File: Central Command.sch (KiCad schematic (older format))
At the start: 18 parts

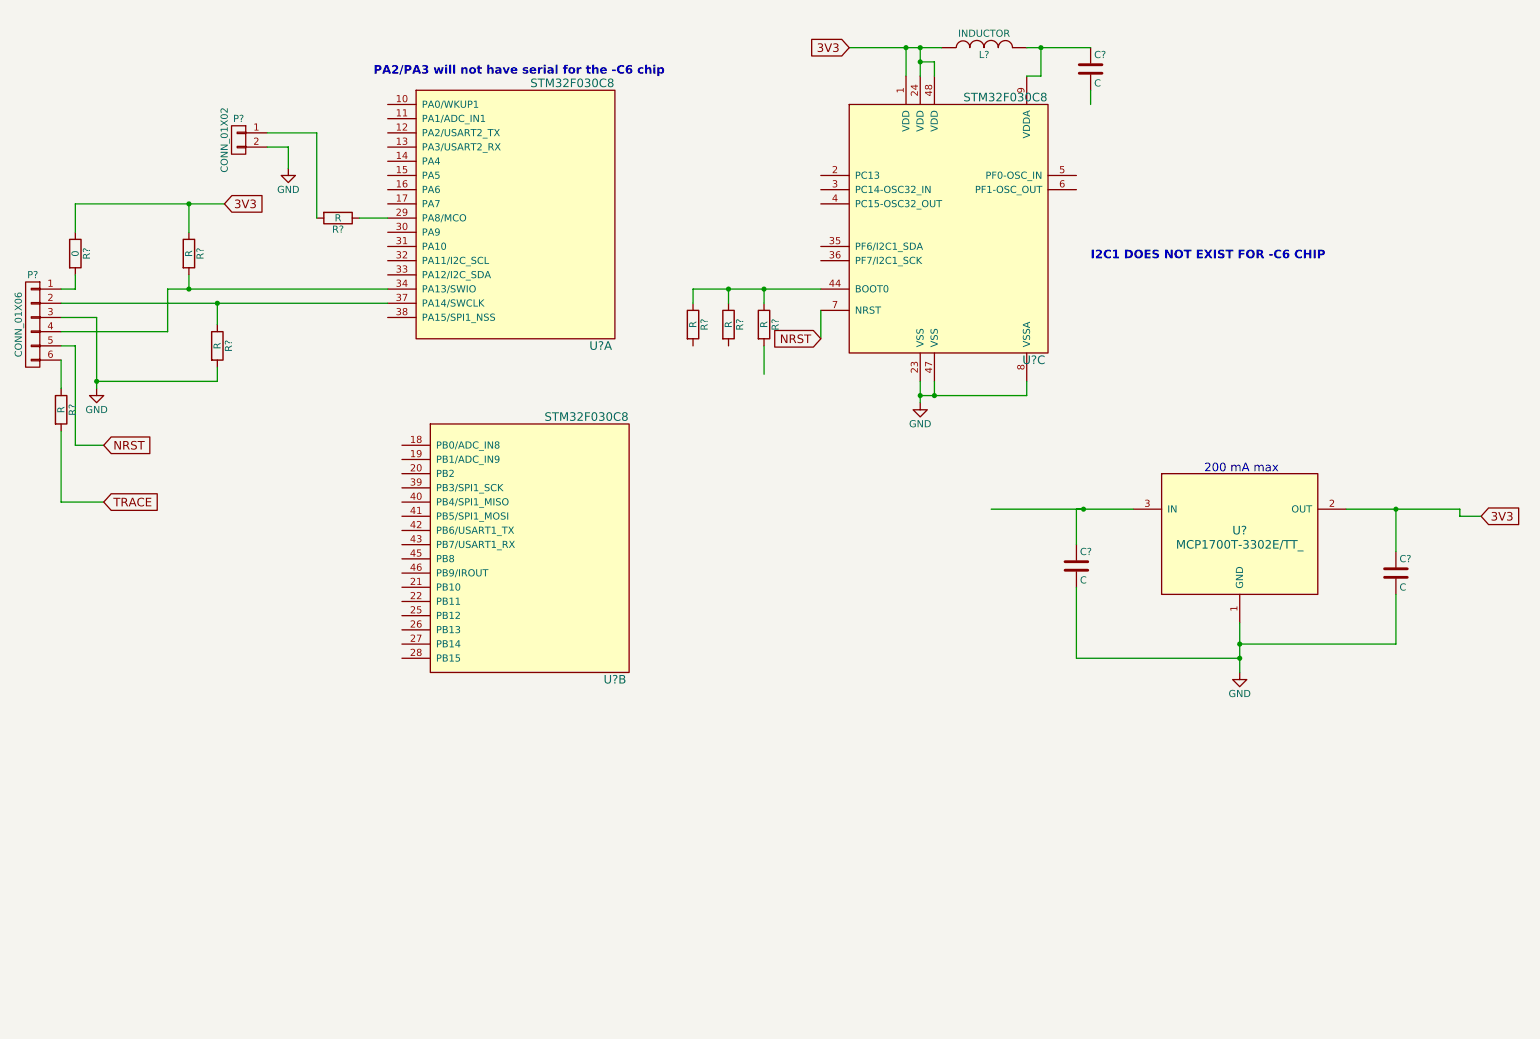
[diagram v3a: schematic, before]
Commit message: Created layout, imported main 48 pin QFP
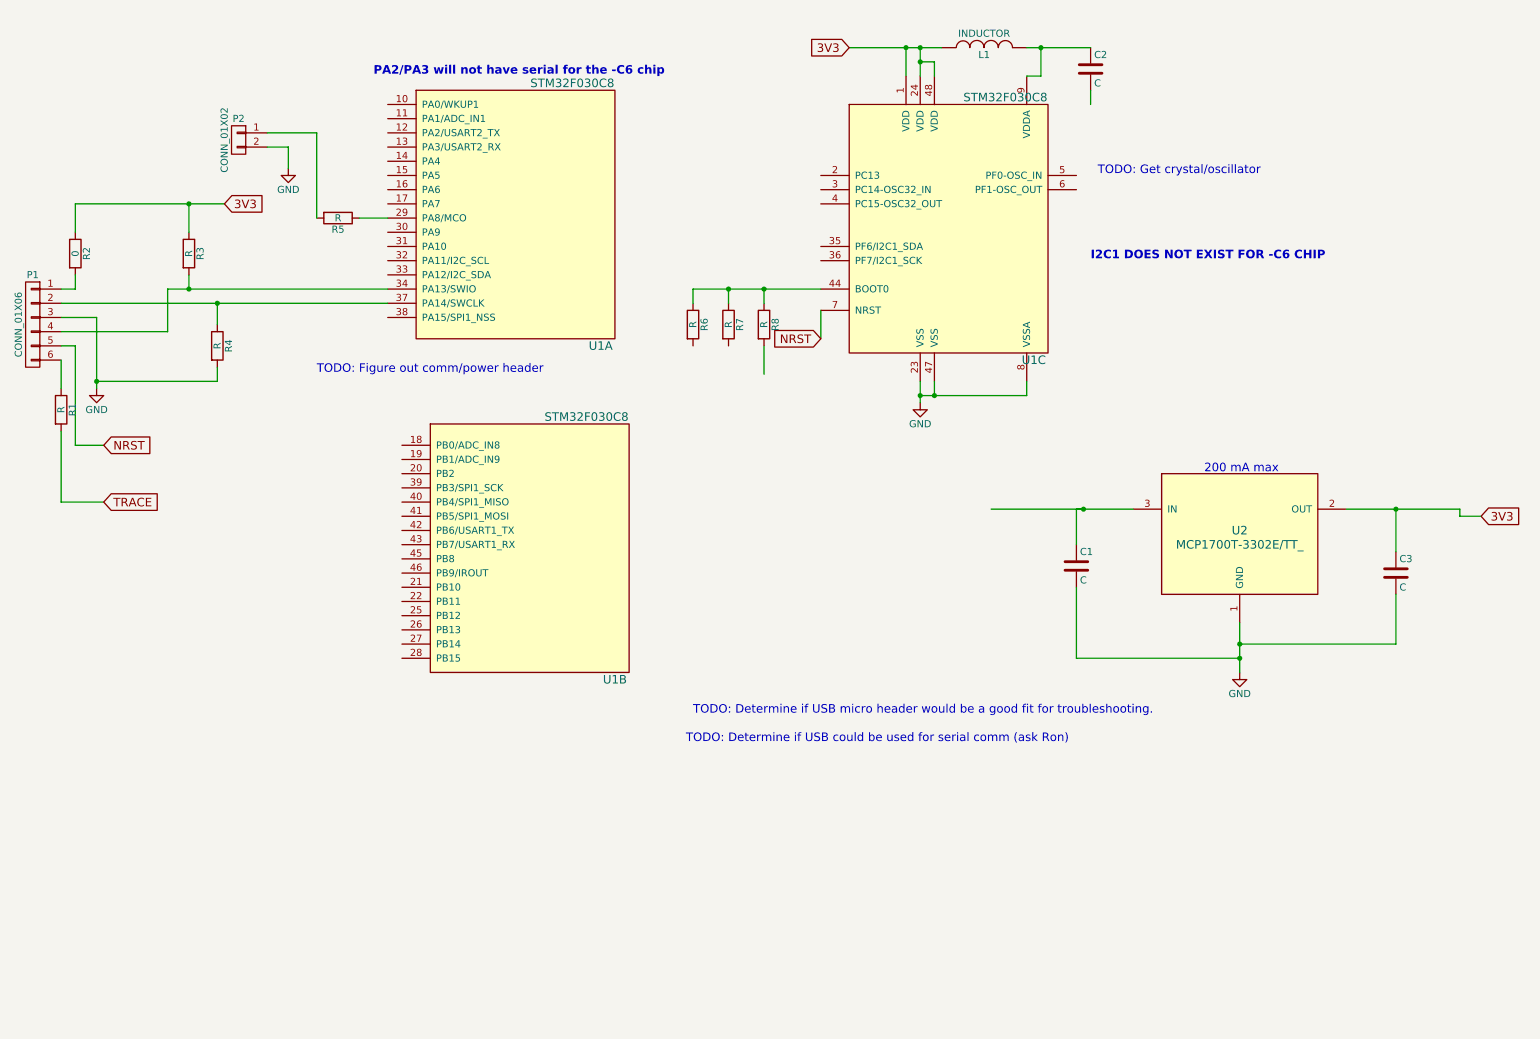
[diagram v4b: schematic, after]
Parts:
- C1, C2, C3: renamed from C?; footprint (none) -> Capacitors_SMD:C_0805
- L1: renamed from L?; footprint (none) -> Inductors_NEOSID:Neosid_Inductor_SM1206
- P1: renamed from P?; footprint (none) -> Pin_Headers:Pin_Header_Straight_1x06
- P2: renamed from P?; footprint (none) -> Pin_Headers:Pin_Header_Straight_1x02
- R1, R2, R3, R4, R5, R6, R7, R8: renamed from R?; footprint (none) -> Resistors_SMD:R_0805
- U1: renamed from U?; footprint (none) -> Housings_QFP:LQFP-48_7x7mm_Pitch0.5mm
- U2: renamed from U?; footprint (none) -> Housings_SOT-23_SOT-143_TSOT-6:SOT-23
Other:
- note added: "TODO: Determine if USB could be used for serial comm (ask Ron)"
- note added: "TODO: Determine if USB micro header would be a good fit for troubleshooting."
- note added: "TODO: Figure out comm/power header"
- note added: "TODO: Get crystal/oscillator"
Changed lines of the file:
@@
 $EndDescr
 $Comp
-L INDUCTOR L?
+L INDUCTOR L1
 U 1 1 5626F24B
 P 7250 800
-F 0 "L?" V 7200 800 50  0000 C CNN
+F 0 "L1" V 7200 800 50  0000 C CNN
 F 1 "INDUCTOR" V 7350 800 50  0000 C CNN
-F 2 "" H 7250 800 60  0000 C CNN
+F 2 "Inductors_NEOSID:Neosid_Inductor_SM1206" H 7250 800 60  0001 C CNN
 F 3 "" H 7250 800 60  0000 C CNN
 	1    7250 800
@@
 $EndComp
 $Comp
-L C C?
+L C C2
 U 1 1 5626F380
 P 8000 950
-F 0 "C?" H 8025 1050 50  0000 L CNN
+F 0 "C2" H 8025 1050 50  0000 L CNN
 F 1 "C" H 8025 850 50  0000 L CNN
-F 2 "" H 8038 800 30  0000 C CNN
+F 2 "Capacitors_SMD:C_0805" H 8038 800 30  0001 C CNN
 F 3 "" H 8000 950 60  0000 C CNN
 	1    8000 950
@@
 $EndComp
 $Comp
-L MCP1700T-3302E/TT_ U?
+L MCP1700T-3302E/TT_ U2
 U 1 1 56270053
 P 9050 4200
-F 0 "U?" H 9050 4200 60  0000 C CNN
+F 0 "U2" H 9050 4200 60  0000 C CNN
 F 1 "MCP1700T-3302E/TT_" H 9050 4100 60  0000 C CNN
-F 2 "" H 9050 4200 60  0000 C CNN
+F 2 "Housings_SOT-23_SOT-143_TSOT-6:SOT-23" H 9050 4200 60  0001 C CNN
 F 3 "" H 9050 4200 60  0000 C CNN
 F 4 "http://parts.io/detail/1370896/MCP1700T-3302E%2FTT" H 9050 4200 60  0001 C CNN "Link"
@@
 $EndComp
 $Comp
-L C C?
+L C C1
 U 1 1 5627009A
 P 7900 4450
-F 0 "C?" H 7925 4550 50  0000 L CNN
+F 0 "C1" H 7925 4550 50  0000 L CNN
 F 1 "C" H 7925 4350 50  0000 L CNN
-F 2 "" H 7938 4300 30  0000 C CNN
+F 2 "Capacitors_SMD:C_0805" H 7938 4300 30  0001 C CNN
 F 3 "" H 7900 4450 60  0000 C CNN
 	1    7900 4450
@@
 $EndComp
 $Comp
-L C C?
+L C C3
 U 1 1 56270119
 P 10150 4500
-F 0 "C?" H 10175 4600 50  0000 L CNN
+F 0 "C3" H 10175 4600 50  0000 L CNN
 F 1 "C" H 10175 4400 50  0000 L CNN
-F 2 "" H 10188 4350 30  0000 C CNN
+F 2 "Capacitors_SMD:C_0805" H 10188 4350 30  0001 C CNN
 F 3 "" H 10150 4500 60  0000 C CNN
 	1    10150 4500
@@
 $EndComp
 $Comp
-L GND #PWR?
+L GND #PWR01
 U 1 1 562701EB
 P 9050 5200
-F 0 "#PWR?" H 9050 4950 50  0001 C CNN
+F 0 "#PWR01" H 9050 4950 50  0001 C CNN
 F 1 "GND" H 9050 5050 50  0000 C CNN
 F 2 "" H 9050 5200 60  0000 C CNN
@@
 3V3
 $Comp
-L GND #PWR?
+L GND #PWR02
 U 1 1 5627066D
 P 6800 3300
-F 0 "#PWR?" H 6800 3050 50  0001 C CNN
+F 0 "#PWR02" H 6800 3050 50  0001 C CNN
 F 1 "GND" H 6800 3150 50  0000 C CNN
 F 2 "" H 6800 3300 60  0000 C CNN
@@
 200 mA max
 $Comp
-L R R?
+L R R8
 U 1 1 562D2D9E
 P 5700 2750
-F 0 "R?" V 5780 2750 50  0000 C CNN
+F 0 "R8" V 5780 2750 50  0000 C CNN
 F 1 "R" V 5700 2750 50  0000 C CNN
-F 2 "" V 5630 2750 30  0000 C CNN
+F 2 "Resistors_SMD:R_0805" V 5630 2750 30  0001 C CNN
 F 3 "" H 5700 2750 30  0000 C CNN
 	1    5700 2750
@@
 $EndComp
 $Comp
-L R R?
+L R R7
 U 1 1 562D2E53
 P 5450 2750
-F 0 "R?" V 5530 2750 50  0000 C CNN
+F 0 "R7" V 5530 2750 50  0000 C CNN
 F 1 "R" V 5450 2750 50  0000 C CNN
-F 2 "" V 5380 2750 30  0000 C CNN
+F 2 "Resistors_SMD:R_0805" V 5380 2750 30  0001 C CNN
 F 3 "" H 5450 2750 30  0000 C CNN
 	1    5450 2750
@@
 $EndComp
 $Comp
-L R R?
+L R R6
 U 1 1 562D2EC7
 P 5200 2750
-F 0 "R?" V 5280 2750 50  0000 C CNN
+F 0 "R6" V 5280 2750 50  0000 C CNN
 F 1 "R" V 5200 2750 50  0000 C CNN
-F 2 "" V 5130 2750 30  0000 C CNN
+F 2 "Resistors_SMD:R_0805" V 5130 2750 30  0001 C CNN
 F 3 "" H 5200 2750 30  0000 C CNN
 	1    5200 2750
@@
 $EndComp
 $Comp
-L CONN_01X06 P?
+L CONN_01X06 P1
 U 1 1 562D3447
 P 550 2750
-F 0 "P?" H 550 3100 50  0000 C CNN
+F 0 "P1" H 550 3100 50  0000 C CNN
 F 1 "CONN_01X06" V 650 2750 50  0000 C CNN
-F 2 "" H 550 2750 60  0000 C CNN
+F 2 "Pin_Headers:Pin_Header_Straight_1x06" H 550 2750 60  0001 C CNN
 F 3 "" H 550 2750 60  0000 C CNN
 	1    550  2750
@@
 	850  1900 850  2100
 $Comp
-L R R?
+L R R2
 U 1 1 562D36B1
 P 850 2250
-F 0 "R?" V 930 2250 50  0000 C CNN
+F 0 "R2" V 930 2250 50  0000 C CNN
 F 1 "0" V 850 2250 50  0000 C CNN
-F 2 "" V 780 2250 30  0000 C CNN
+F 2 "Resistors_SMD:R_0805" V 780 2250 30  0001 C CNN
 F 3 "" H 850 2250 30  0000 C CNN
 	1    850  2250
@@
 	850  2500 750  2500
 $Comp
-L GND #PWR?
+L GND #PWR03
 U 1 1 562D38AD
 P 1000 3200
-F 0 "#PWR?" H 1000 2950 50  0001 C CNN
+F 0 "#PWR03" H 1000 2950 50  0001 C CNN
 F 1 "GND" H 1000 3050 50  0000 C CNN
 F 2 "" H 1000 3200 60  0000 C CNN
@@
 	6100 2650 6100 2850
 $Comp
-L R R?
+L R R4
 U 1 1 562D3B38
 P 1850 2900
-F 0 "R?" V 1930 2900 50  0000 C CNN
+F 0 "R4" V 1930 2900 50  0000 C CNN
 F 1 "R" V 1850 2900 50  0000 C CNN
-F 2 "" V 1780 2900 30  0000 C CNN
+F 2 "Resistors_SMD:R_0805" V 1780 2900 30  0001 C CNN
 F 3 "" H 1850 2900 30  0000 C CNN
 	1    1850 2900
@@
 $EndComp
 $Comp
-L R R?
+L R R3
 U 1 1 562D3B9C
 P 1650 2250
-F 0 "R?" V 1730 2250 50  0000 C CNN
+F 0 "R3" V 1730 2250 50  0000 C CNN
 F 1 "R" V 1650 2250 50  0000 C CNN
-F 2 "" V 1580 2250 30  0000 C CNN
+F 2 "Resistors_SMD:R_0805" V 1580 2250 30  0001 C CNN
 F 3 "" H 1650 2250 30  0000 C CNN
 	1    1650 2250
@@
 Connection ~ 1850 2600
 $Comp
-L R R?
+L R R1
 U 1 1 562D411E
 P 750 3350
-F 0 "R?" V 830 3350 50  0000 C CNN
+F 0 "R1" V 830 3350 50  0000 C CNN
 F 1 "R" V 750 3350 50  0000 C CNN
-F 2 "" V 680 3350 30  0000 C CNN
+F 2 "Resistors_SMD:R_0805" V 680 3350 30  0001 C CNN
 F 3 "" H 750 3350 30  0000 C CNN
 	1    750  3350
@@
 I2C1 DOES NOT EXIST FOR -C6 CHIP
 $Comp
-L R R?
+L R R5
 U 1 1 562D4FA8
 P 2700 2000
-F 0 "R?" V 2780 2000 50  0000 C CNN
+F 0 "R5" V 2780 2000 50  0000 C CNN
 F 1 "R" V 2700 2000 50  0000 C CNN
-F 2 "" V 2630 2000 30  0000 C CNN
+F 2 "Resistors_SMD:R_0805" V 2630 2000 30  0001 C CNN
 F 3 "" H 2700 2000 30  0000 C CNN
 	1    2700 2000
@@
 	2850 2000 3050 2000
 $Comp
-L CONN_01X02 P?
+L CONN_01X02 P2
 U 1 1 562D514A
 P 2000 1450
-F 0 "P?" H 2000 1600 50  0000 C CNN
+F 0 "P2" H 2000 1600 50  0000 C CNN
 F 1 "CONN_01X02" V 2100 1450 50  0000 C CNN
-F 2 "" H 2000 1450 60  0000 C CNN
+F 2 "Pin_Headers:Pin_Header_Straight_1x02" H 2000 1450 60  0001 C CNN
 F 3 "" H 2000 1450 60  0000 C CNN
 	1    2000 1450
@@
 	2350 1500 2350 1650
 $Comp
-L GND #PWR?
+L GND #PWR04
 U 1 1 562D543E
 P 2350 1650
-F 0 "#PWR?" H 2350 1400 50  0001 C CNN
+F 0 "#PWR04" H 2350 1400 50  0001 C CNN
 F 1 "GND" H 2350 1500 50  0000 C CNN
 F 2 "" H 2350 1650 60  0000 C CNN
@@
 PA2/PA3 will not have serial for the -C6 chip
 $Comp
-L STM32F030C8 U?
+L STM32F030C8 U1
 U 1 1 564E875E
 P 4000 1950
-F 0 "U?" H 4550 1000 60  0000 C CNN
+F 0 "U1" H 4550 1000 60  0000 C CNN
 F 1 "STM32F030C8" H 4350 2850 60  0000 C CNN
-F 2 "" H 4000 1950 60  0000 C CNN
+F 2 "Housings_QFP:LQFP-48_7x7mm_Pitch0.5mm" H 4000 1950 60  0001 C CNN
 F 3 "" H 4000 1950 60  0000 C CNN
 	1    4000 1950
@@
 $EndComp
 $Comp
-L STM32F030C8 U?
+L STM32F030C8 U1
 U 2 1 564E8A03
 P 4100 4300
-F 0 "U?" H 4650 3350 60  0000 C CNN
+F 0 "U1" H 4650 3350 60  0000 C CNN
 F 1 "STM32F030C8" H 4450 5200 60  0000 C CNN
-F 2 "" H 4100 4300 60  0000 C CNN
+F 2 "Housings_QFP:LQFP-48_7x7mm_Pitch0.5mm" H 4100 4300 60  0001 C CNN
 F 3 "" H 4100 4300 60  0000 C CNN
 	2    4100 4300
@@
 $EndComp
 $Comp
-L STM32F030C8 U?
+L STM32F030C8 U1
 U 3 1 564E8FF6
 P 7050 2050
-F 0 "U?" H 7600 1100 60  0000 C CNN
+F 0 "U1" H 7600 1100 60  0000 C CNN
 F 1 "STM32F030C8" H 7400 2950 60  0000 C CNN
-F 2 "" H 7050 2050 60  0000 C CNN
+F 2 "Housings_QFP:LQFP-48_7x7mm_Pitch0.5mm" H 7050 2050 60  0001 C CNN
 F 3 "" H 7050 2050 60  0000 C CNN
 	3    7050 2050
 	1    0    0    -1
 $EndComp
+Text Notes 8050 1700 0    60   ~ 0
+TODO: Get crystal/oscillator
+Text Notes 2550 3100 0    60   ~ 0
+TODO: Figure out comm/power header
+Text Notes 5200 5500 0    60   ~ 0
+TODO: Determine if USB micro header would be a good fit for troubleshooting.
+Text Notes 5150 5700 0    60   ~ 0
+TODO: Determine if USB could be used for serial comm (ask Ron)
 $EndSCHEMATC
